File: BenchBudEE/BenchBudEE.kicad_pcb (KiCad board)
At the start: 2 copper layers, 0 parts

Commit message: Parts added to relay module. Schematic tidied up.
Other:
- rule trace_min: 0.254 -> 0.1524
- rule via_min_drill: 0.508 -> 0.3302
- rule via_min_size: 0.889 -> 0.508
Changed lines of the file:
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@@
     (zone_clearance 0.508)
     (zone_45_only no)
-    (trace_min 0.254)
+    (trace_min 0.1524)
     (segment_width 0.2)
     (edge_width 0.1)
     (via_size 0.889)
     (via_drill 0.635)
-    (via_min_size 0.889)
-    (via_min_drill 0.508)
+    (via_min_size 0.508)
+    (via_min_drill 0.3302)
     (uvia_size 0.508)
     (uvia_drill 0.127)
     (uvias_allowed no)
-    (uvia_min_size 0.508)
+    (uvia_min_size 0.381)
     (uvia_min_drill 0.127)
     (pcb_text_width 0.3)
@@
     (pad_to_mask_clearance 0)
     (aux_axis_origin 0 0)
-    (visible_elements FFFFFFBF)
+    (visible_elements 7FFFFFFF)
     (pcbplotparams
       (layerselection 3178497)

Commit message: Design rules specified for layout.
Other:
- board outline added: 165.1 x 63.5 mm
- copper layers 2 -> 4
- rule pad_to_mask_clearance: 0 -> 0.254
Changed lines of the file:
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@@
     (area 0 0 0 0)
     (thickness 1.6)
-    (drawings 0)
+    (drawings 5)
     (tracks 0)
     (zones 0)
@@
     (nets 1)
   )
-  (page A3)
+  (page A4)
+  (title_block
+    (title BenchBudEE)
+    (rev A)
+    (company "Contextual Electronics")
+  )
   (layers
     (15 F.Cu signal)
+    (2 PWR power)
+    (1 GND power)
     (0 B.Cu signal)
     (16 B.Adhes user)
@@
     (22 B.Mask user)
     (23 F.Mask user)
-    (24 Dwgs.User user)
-    (25 Cmts.User user)
-    (26 Eco1.User user)
-    (27 Eco2.User user)
     (28 Edge.Cuts user)
   )
   (setup
-    (last_trace_width 0.254)
+    (last_trace_width 0.1524)
+    (user_trace_width 0.1524)
     (trace_clearance 0.254)
     (zone_clearance 0.508)
@@
     (via_min_size 0.508)
     (via_min_drill 0.3302)
+    (user_via 0.508 0.3302)
     (uvia_size 0.508)
     (uvia_drill 0.127)
@@
     (mod_text_size 1 1)
     (mod_text_width 0.15)
-    (pad_size 1.5 1.5)
-    (pad_drill 0.6)
-    (pad_to_mask_clearance 0)
+    (pad_size 2 2)
+    (pad_drill 1.3)
+    (pad_to_mask_clearance 0.254)
+    (solder_mask_min_width 0.127)
     (aux_axis_origin 0 0)
     (visible_elements 7FFFFFFF)
@@
     (add_net "")
   )
+  (gr_line (start 213.36 68.58) (end 48.26 68.58) (angle 90) (layer Edge.Cuts) (width 0.1))
+  (gr_line (start 213.36 132.08) (end 213.36 68.58) (angle 90) (layer Edge.Cuts) (width 0.1))
+  (gr_line (start 200.66 132.08) (end 213.36 132.08) (angle 90) (layer Edge.Cuts) (width 0.1))
+  (gr_line (start 48.26 132.08) (end 200.66 132.08) (angle 90) (layer Edge.Cuts) (width 0.1))
+  (gr_line (start 48.26 68.58) (end 48.26 132.08) (angle 90) (layer Edge.Cuts) (width 0.1))
 )

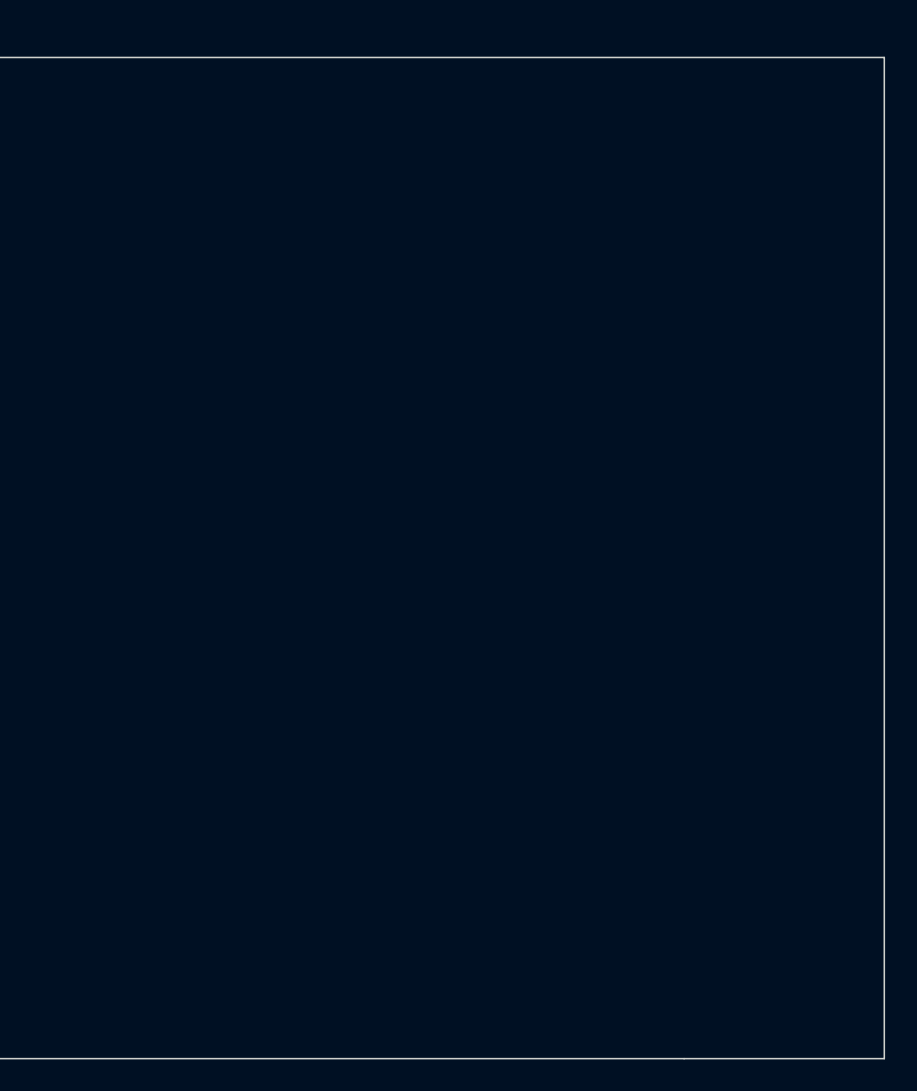
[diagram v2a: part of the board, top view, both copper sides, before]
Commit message: Parts added to thermocouple module. Relay & thermocouple rough placement.
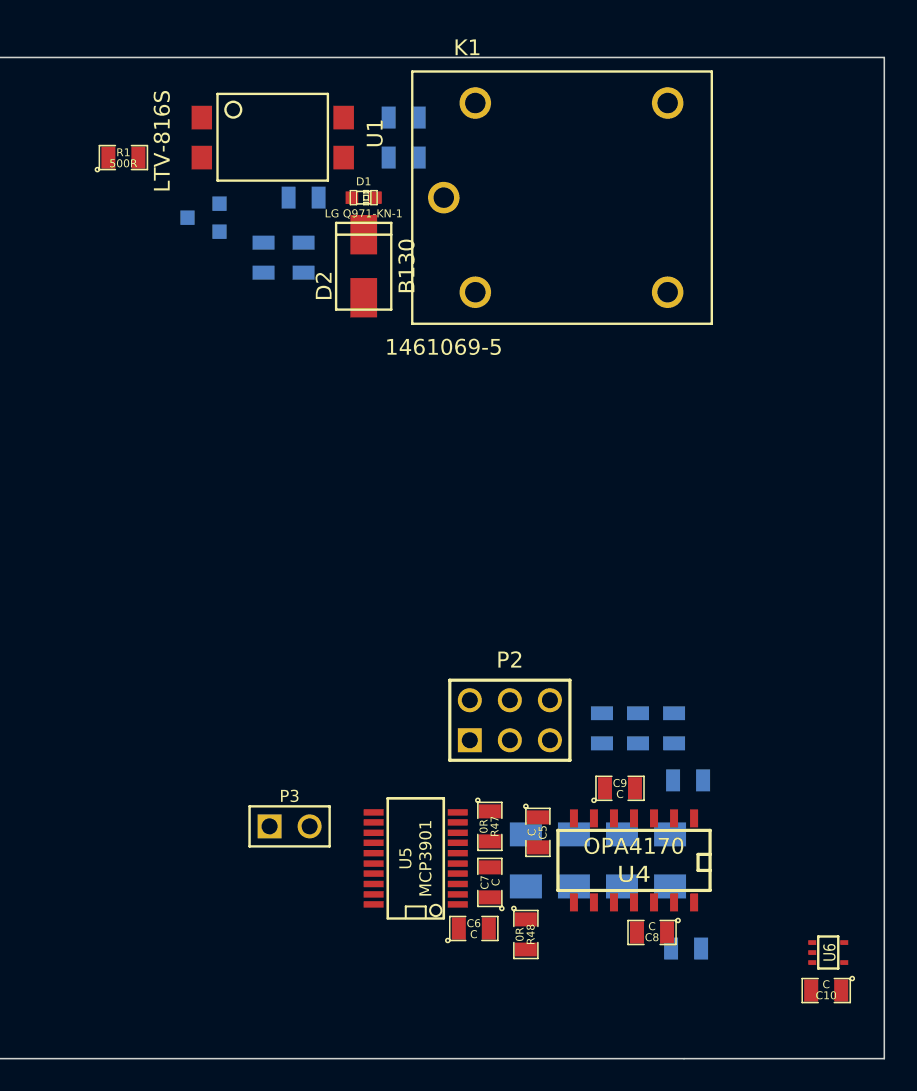
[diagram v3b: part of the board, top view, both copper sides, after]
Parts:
- added C10: C, SM0805, F.Cu at (209.7, 127.8)
- added C5: C, SM0805, F.Cu at (191.4, 117.7)
- added C6: C, SM0805, F.Cu at (187.3, 123.8)
- added C7: C, SM0805, F.Cu at (188.3, 120.9)
- added C8: C, SM0805, F.Cu at (198.6, 124.1)
- added C9: C, SM0805, F.Cu at (196.6, 114.9)
- added D1: LG Q971-KN-1, LED-0603, F.Cu at (180.3, 77.5)
- added D2: B130, SMA, F.Cu at (180.3, 83.8)
- added K1: 1461069-5, TE-SPDT, F.Cu at (185.4, 77.5)
- added P2: CONN_3X2, pin_array_3x2, F.Cu at (189.6, 110.6)
- added P3: CONN_2, PIN_ARRAY_2X1, F.Cu at (175.6, 117.3)
- added Q1: 2N3904, SOT23EBC, B.Cu at (170.2, 78.7)
- added R1: 500R, SM0805, F.Cu at (165.1, 74.9)
- added R12: R, SM1206, B.Cu at (193.7, 119.5)
- added R13: R, SM1206, B.Cu at (190.6, 119.5)
- added R14: R, SM1206, B.Cu at (196.7, 119.5)
- added R15: R, SM1206, B.Cu at (199.8, 119.5)
- added R16: R, SM0805, B.Cu at (200.8, 125.1)
- added R17: R, SM0805, B.Cu at (195.5, 111.1)
- added R18: R, SM0805, B.Cu at (200.9, 114.4)
- added R2: 200R, SM0805, B.Cu at (176.5, 81.3)
- added R3: 0R, SM0805, B.Cu at (182.9, 72.4)
- added R4: 100R, SM0805, B.Cu at (176.5, 77.5)
- added R44: R, SM0805, B.Cu at (200.0, 111.1)
- added R45: R, SM0805, B.Cu at (197.7, 111.1)
- added R47: 0R, SM0805, F.Cu at (188.3, 117.3)
- added R48: 0R, SM0805, F.Cu at (190.6, 124.2)
- added R5: 0R, SM0805, B.Cu at (182.9, 74.9)
- added R6: 0R, SM0805, B.Cu at (174.0, 81.3)
- added U1: LTV-816S, 4-SMD, F.Cu at (179.1, 72.4)
- added U4: OPA4170, SO14E, F.Cu at (197.5, 119.6)
- added U5: MCP3901, SSOP20, F.Cu at (183.6, 119.4)
- added U6: LMT84, SOT353, F.Cu at (209.8, 125.3)

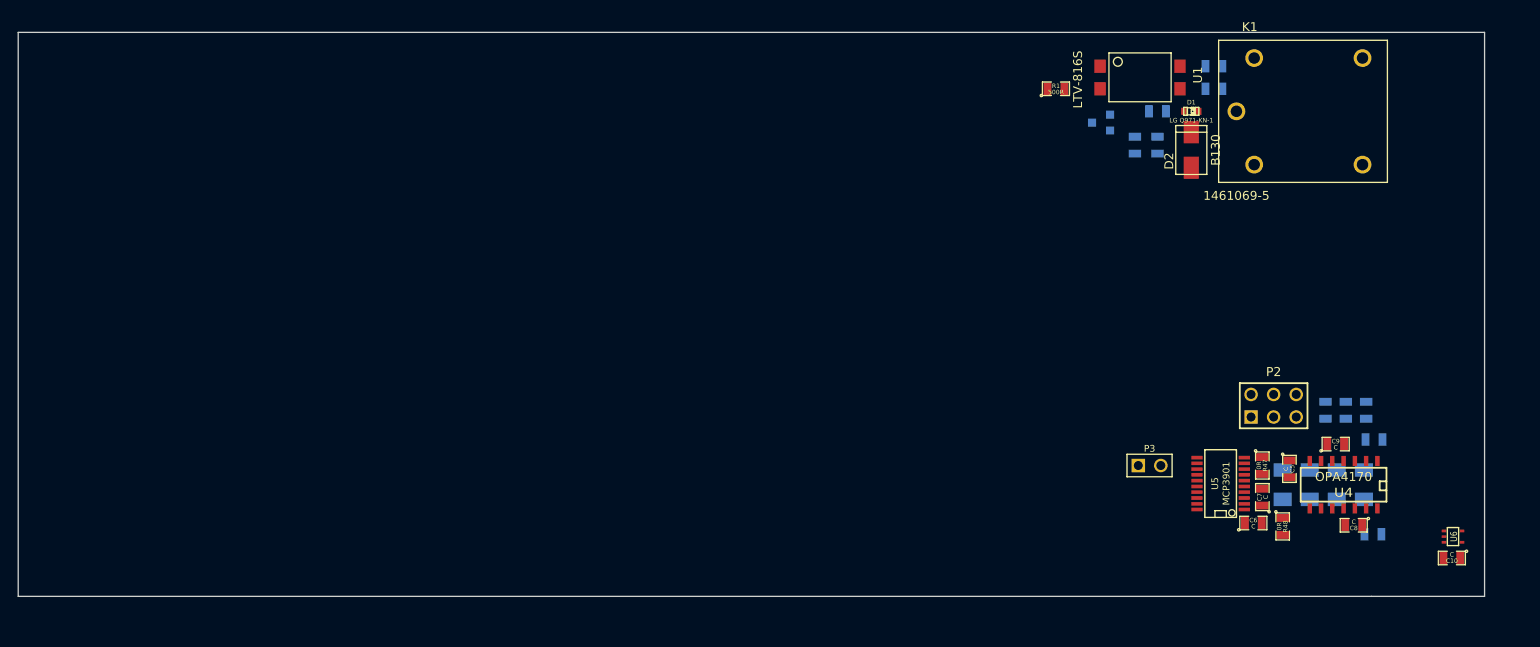
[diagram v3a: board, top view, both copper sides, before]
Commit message: Connectors added + associated + roughly placed.
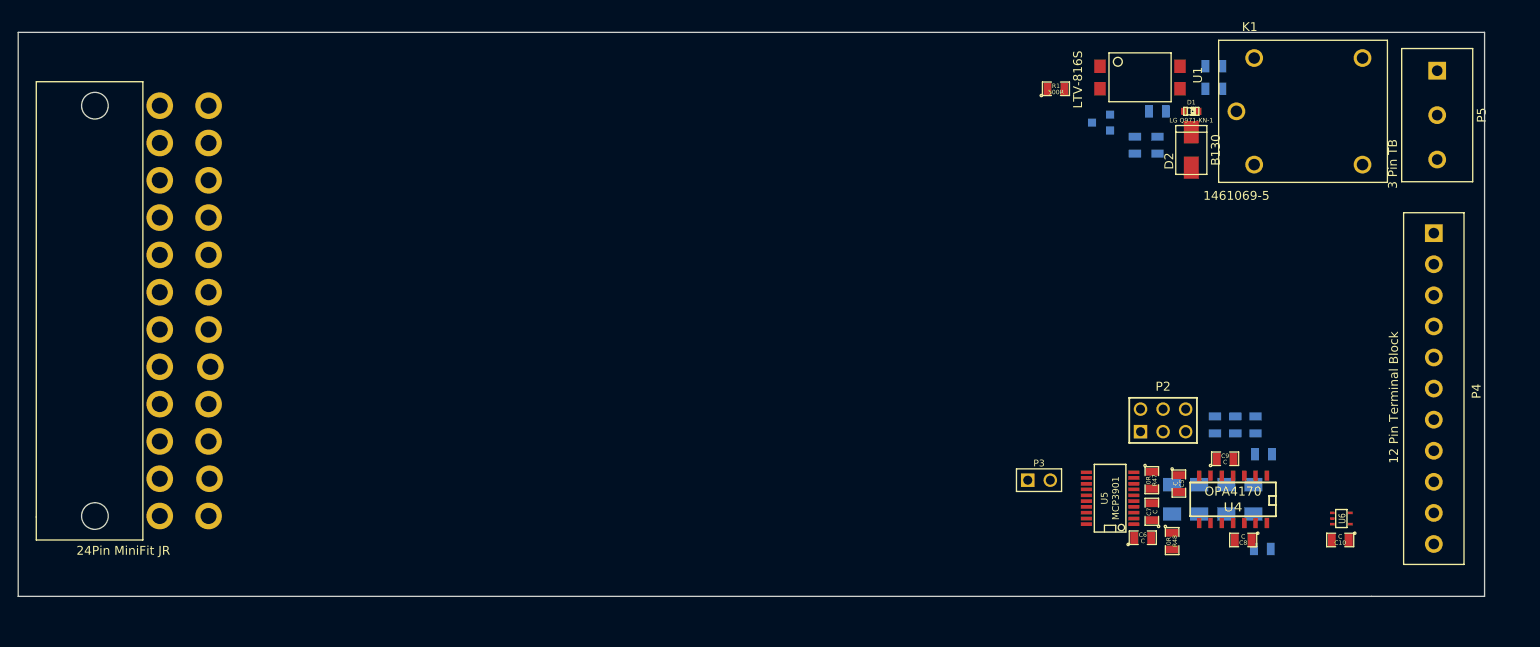
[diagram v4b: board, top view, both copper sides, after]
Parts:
- added P1: 24Pin MiniFit JR, ATX_24Header, F.Cu at (56.9, 76.8)
- added P4: 12 Pin Terminal Block, 12_PIN_TB, F.Cu at (207.6, 91.2)
- added P5: 3 Pin TB, 3_PIN_TB, F.Cu at (208.0, 72.9)
- moved U6 12.7 mm to (197.2, 123.3)
- moved C10 12.7 mm to (197.1, 125.7)
- moved R14 12.6 mm to (184.3, 121.2)
- moved U4 12.6 mm to (185.0, 121.3)
- moved C5 12.6 mm to (178.9, 119.4)
- moved C6 12.6 mm to (174.9, 125.5)
- moved C7 12.6 mm to (175.9, 122.6)
- moved C8 12.6 mm to (186.2, 125.7)
- moved C9 12.6 mm to (184.2, 116.6)
- moved P2 12.6 mm to (177.2, 112.3)
- moved P3 12.6 mm to (163.2, 119.0)
- moved R12 12.6 mm to (181.2, 121.2)
- moved R13 12.6 mm to (178.2, 121.2)
- moved R15 12.6 mm to (187.3, 121.2)
- moved R16 12.6 mm to (188.3, 126.7)
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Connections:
- K1 pad 1: (no net) -> /Relay/RELAY_COM
- K1 pad 3: (no net) -> /Relay/RELAY_NO
- K1 pad 4: (no net) -> /Relay/RELAY_NC
- U4 pad 12: (no net) -> /Thermocouple/TC IN+
- U4 pad 3: (no net) -> /Thermocouple/TC IN-

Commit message: Arduino module associated + roughly placed.
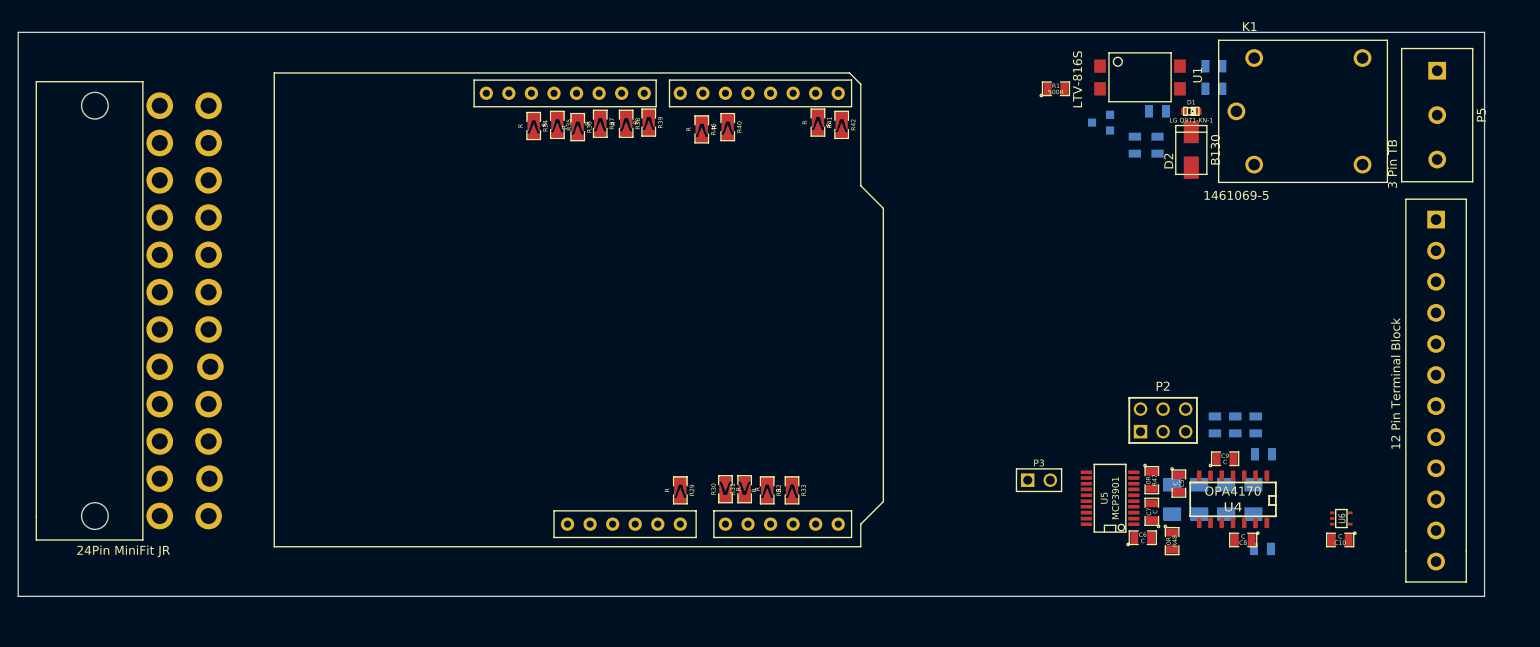
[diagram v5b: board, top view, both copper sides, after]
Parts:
- added ARD1: ARDUINOPINS, ARDUINO_UNO_HE, F.Cu at (140.6, 124.0)
- added R29: R, SM0805_SolderBridge, F.Cu at (122.8, 120.1)
- added R30: R, SM0805_SolderBridge, F.Cu at (127.9, 120.0)
- added R31: R, SM0805_SolderBridge, F.Cu at (130.0, 120.0)
- added R32: R, SM0805_SolderBridge, F.Cu at (132.6, 120.1)
- added R33: R, SM0805_SolderBridge, F.Cu at (135.4, 120.1)
- added R34: R, SM0805_SolderBridge, F.Cu at (106.3, 79.1)
- added R35: R, SM0805_SolderBridge, F.Cu at (109.0, 79.0)
- added R36: R, SM0805_SolderBridge, F.Cu at (111.3, 79.2)
- added R37: R, SM0805_SolderBridge, F.Cu at (113.8, 78.9)
- added R38: R, SM0805_SolderBridge, F.Cu at (116.7, 78.9)
- added R39: R, SM0805_SolderBridge, F.Cu at (119.3, 78.7)
- added R40: R, SM0805_SolderBridge, F.Cu at (128.1, 79.2)
- added R41: R, SM0805_SolderBridge, F.Cu at (138.3, 78.7)
- added R42: R, SM0805_SolderBridge, F.Cu at (141.0, 79.0)
- added R46: R, SM0805_SolderBridge, F.Cu at (125.2, 79.5)
- moved P4 1.55 mm to (207.9, 89.7)

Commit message: Modified 0805 SB footprint.
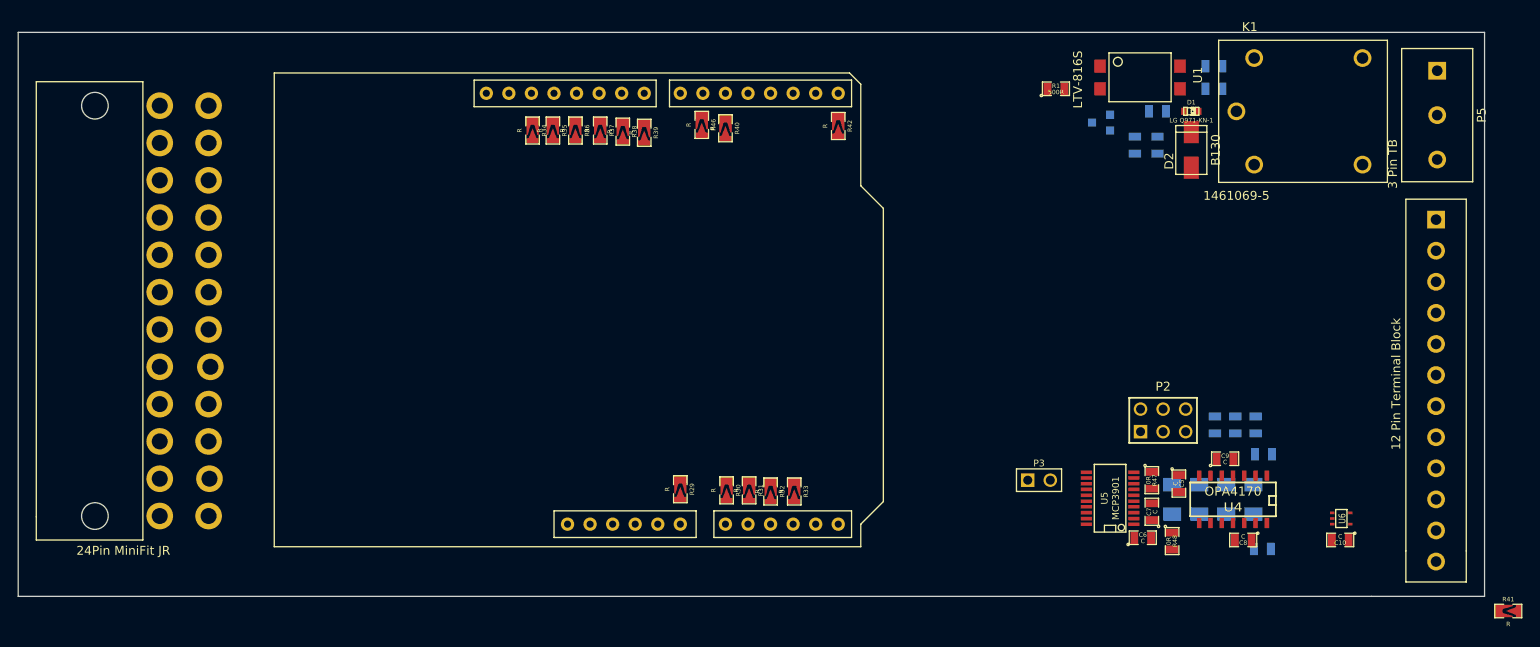
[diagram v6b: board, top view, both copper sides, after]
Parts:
- moved R41 95.2 mm to (216.0, 133.7), turned to 0 degrees
- moved R39 1.25 mm to (118.7, 79.9)
- moved R38 0.97 mm to (116.3, 79.8)
- moved R35 0.81 mm to (108.5, 79.6)
- moved R37 0.76 mm to (113.8, 79.6)
- moved R34 0.52 mm to (106.2, 79.6)
- moved R31 0.52 mm to (130.6, 120.1), turned to 270 degrees
- moved R46 0.51 mm to (125.2, 79.0)
- moved R36 0.46 mm to (111.0, 79.6)
- moved R32 0.40 mm to (133.0, 120.3)
- moved R42 0.40 mm to (140.6, 79.1)
- moved R40 0.28 mm to (127.9, 79.4)
- moved R33 0.28 mm to (135.6, 120.3)
- moved R30 0.18 mm to (128.0, 120.1), turned to 270 degrees
- moved R29 0.13 mm to (122.8, 120.0)

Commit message: Fan/Current driver associated + roughly placed.
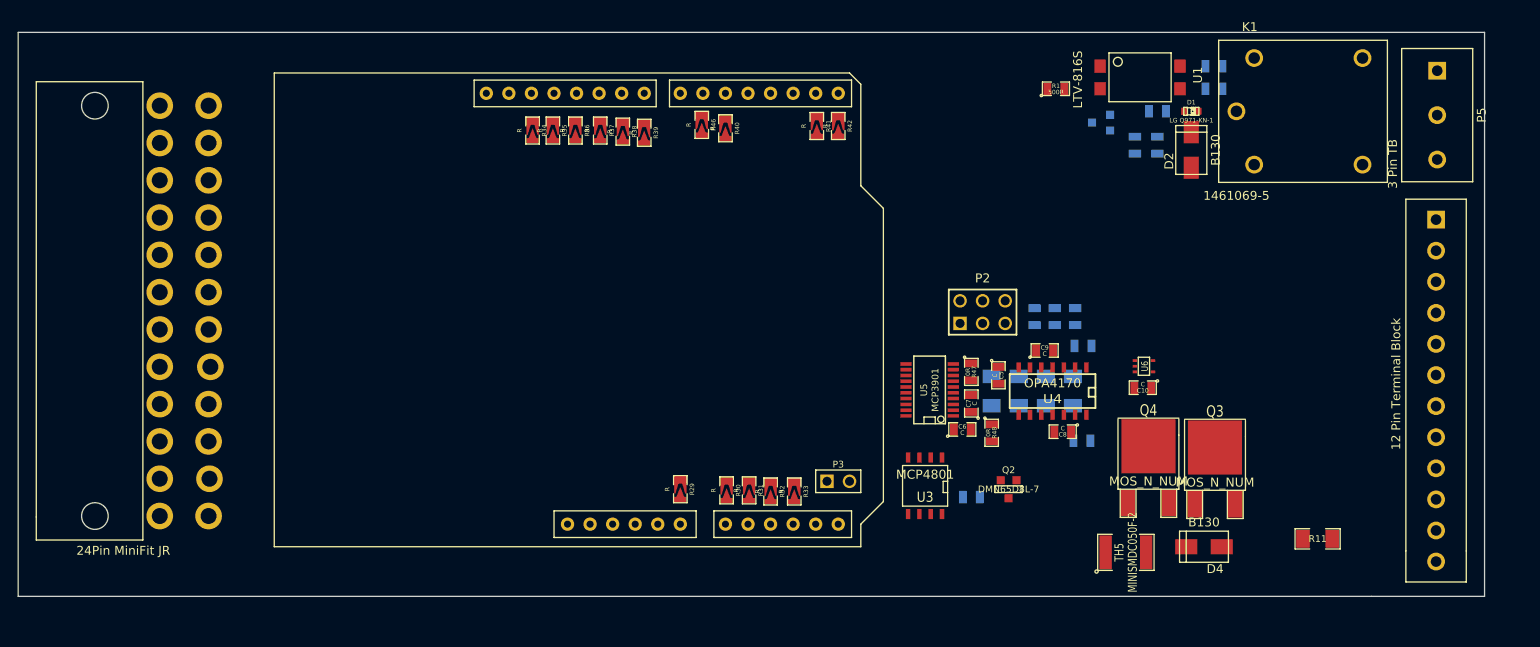
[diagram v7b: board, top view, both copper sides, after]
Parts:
- added D4: B130, SMA, F.Cu at (183.8, 126.5)
- added Q2: DMN65D8L-7, SOT23GDS, F.Cu at (159.8, 120.0)
- added Q3: MOS_N_NUM, DPAK2, F.Cu at (183.0, 121.7)
- added Q4: MOS_N_NUM, DPAK2, F.Cu at (175.5, 121.5)
- added R10: R, SM0805, B.Cu at (155.6, 120.9)
- added R11: R, SM1206, F.Cu at (194.6, 125.6)
- added TH5: MINISMDC050F-2, SM1812, F.Cu at (173.0, 127.1)
- added U3: MCP4801, SO8N, F.Cu at (150.4, 119.6)
- moved R41 95.1 mm to (138.2, 79.1), turned to 270 degrees
- moved C10 28.1 mm to (174.9, 108.6)
- moved U6 28.1 mm to (175.0, 106.2)
- moved C7 23.7 mm to (155.6, 110.4)
- moved R12 23.7 mm to (160.9, 109.0)
- moved R13 23.7 mm to (157.9, 109.0)
- moved C5 23.7 mm to (158.6, 107.2)
- moved R16 23.7 mm to (168.0, 114.6)
- moved R44 23.7 mm to (167.3, 100.6)
- moved R47 23.7 mm to (155.6, 106.8)
- moved R48 23.7 mm to (157.9, 113.7)
- moved C8 23.7 mm to (165.9, 113.5)
- moved P2 23.7 mm to (156.8, 100.1)
- moved R14 23.7 mm to (164.0, 109.0)
- moved R15 23.7 mm to (167.0, 109.0)
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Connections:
- net /Arduino/ADC_CS_N renamed /Arduino/~ADC_CS
- ARD1 pad 16: (no net) -> N-0000075
- ARD1 pad 17: (no net) -> N-0000076
- ARD1 pad 20: (no net) -> N-0000085
